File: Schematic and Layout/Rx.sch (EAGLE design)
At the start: 19 parts

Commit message: Add files via upload
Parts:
- U$10: value RES -> 100
- U$11, U$4: value RES -> 10K
- U$13: value LED_1206 -> LED_12V
- U$14: value CAP -> 470uF
- U$15: value RES -> 330
- U$16, U$6: value RES -> 1K
- U$18: value POWER_CONN -> 5V-12V
- U$20: value DIODE_Z_1005 -> 15V_Z
- U$5, U$7: value RES -> 100K
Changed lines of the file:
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@@
 <part name="GND1" library="supply1" deviceset="GND" device=""/>
 <part name="U$3" library="Gas_Sensor_Lib_v1" deviceset="DIODE_1206" device=""/>
-<part name="U$4" library="Gas_Sensor_Lib_v1" deviceset="RES" device=""/>
-<part name="U$5" library="Gas_Sensor_Lib_v1" deviceset="RES" device=""/>
-<part name="U$6" library="Gas_Sensor_Lib_v1" deviceset="RES" device=""/>
-<part name="U$7" library="Gas_Sensor_Lib_v1" deviceset="RES" device=""/>
+<part name="U$4" library="Gas_Sensor_Lib_v1" deviceset="RES" device="" value="10K"/>
+<part name="U$5" library="Gas_Sensor_Lib_v1" deviceset="RES" device="" value="100K"/>
+<part name="U$6" library="Gas_Sensor_Lib_v1" deviceset="RES" device="" value="1K"/>
+<part name="U$7" library="Gas_Sensor_Lib_v1" deviceset="RES" device="" value="100K"/>
 <part name="U$8" library="Gas_Sensor_Lib_v1" deviceset="POWER_CONN" device=""/>
 <part name="GND2" library="supply1" deviceset="GND" device=""/>
 <part name="U$9" library="Gas_Sensor_Lib_v1" deviceset="ESP8266" device=""/>
 <part name="GND3" library="supply1" deviceset="GND" device=""/>
-<part name="U$10" library="Gas_Sensor_Lib_v1" deviceset="RES" device=""/>
-<part name="U$11" library="Gas_Sensor_Lib_v1" deviceset="RES" device=""/>
+<part name="U$10" library="Gas_Sensor_Lib_v1" deviceset="RES" device="" value="100"/>
+<part name="U$11" library="Gas_Sensor_Lib_v1" deviceset="RES" device="" value="10K"/>
 <part name="U$12" library="Gas_Sensor_Lib_v1" deviceset="BUTTON" device=""/>
-<part name="U$13" library="Gas_Sensor_Lib_v1" deviceset="LED_1206" device=""/>
+<part name="U$13" library="Gas_Sensor_Lib_v1" deviceset="LED_1206" device="" value="LED_12V"/>
 <part name="GND4" library="supply1" deviceset="GND" device=""/>
-<part name="U$14" library="Gas_Sensor_Lib_v1" deviceset="CAP" device=""/>
-<part name="U$15" library="Gas_Sensor_Lib_v1" deviceset="RES" device=""/>
-<part name="U$16" library="Gas_Sensor_Lib_v1" deviceset="RES" device=""/>
+<part name="U$14" library="Gas_Sensor_Lib_v1" deviceset="CAP" device="" value="470uF"/>
+<part name="U$15" library="Gas_Sensor_Lib_v1" deviceset="RES" device="" value="330"/>
+<part name="U$16" library="Gas_Sensor_Lib_v1" deviceset="RES" device="" value="1K"/>
 <part name="U$17" library="Gas_Sensor_Lib_v1" deviceset="DIODE_1206" device=""/>
-<part name="U$18" library="Gas_Sensor_Lib_v1" deviceset="POWER_CONN" device=""/>
-<part name="U$20" library="Gas_Sensor_Lib_v1" deviceset="DIODE_Z_1005" device=""/>
+<part name="U$18" library="Gas_Sensor_Lib_v1" deviceset="POWER_CONN" device="" value="5V-12V"/>
+<part name="U$20" library="Gas_Sensor_Lib_v1" deviceset="DIODE_Z_1005" device="" value="15V_Z"/>
 </parts>
 <sheets>

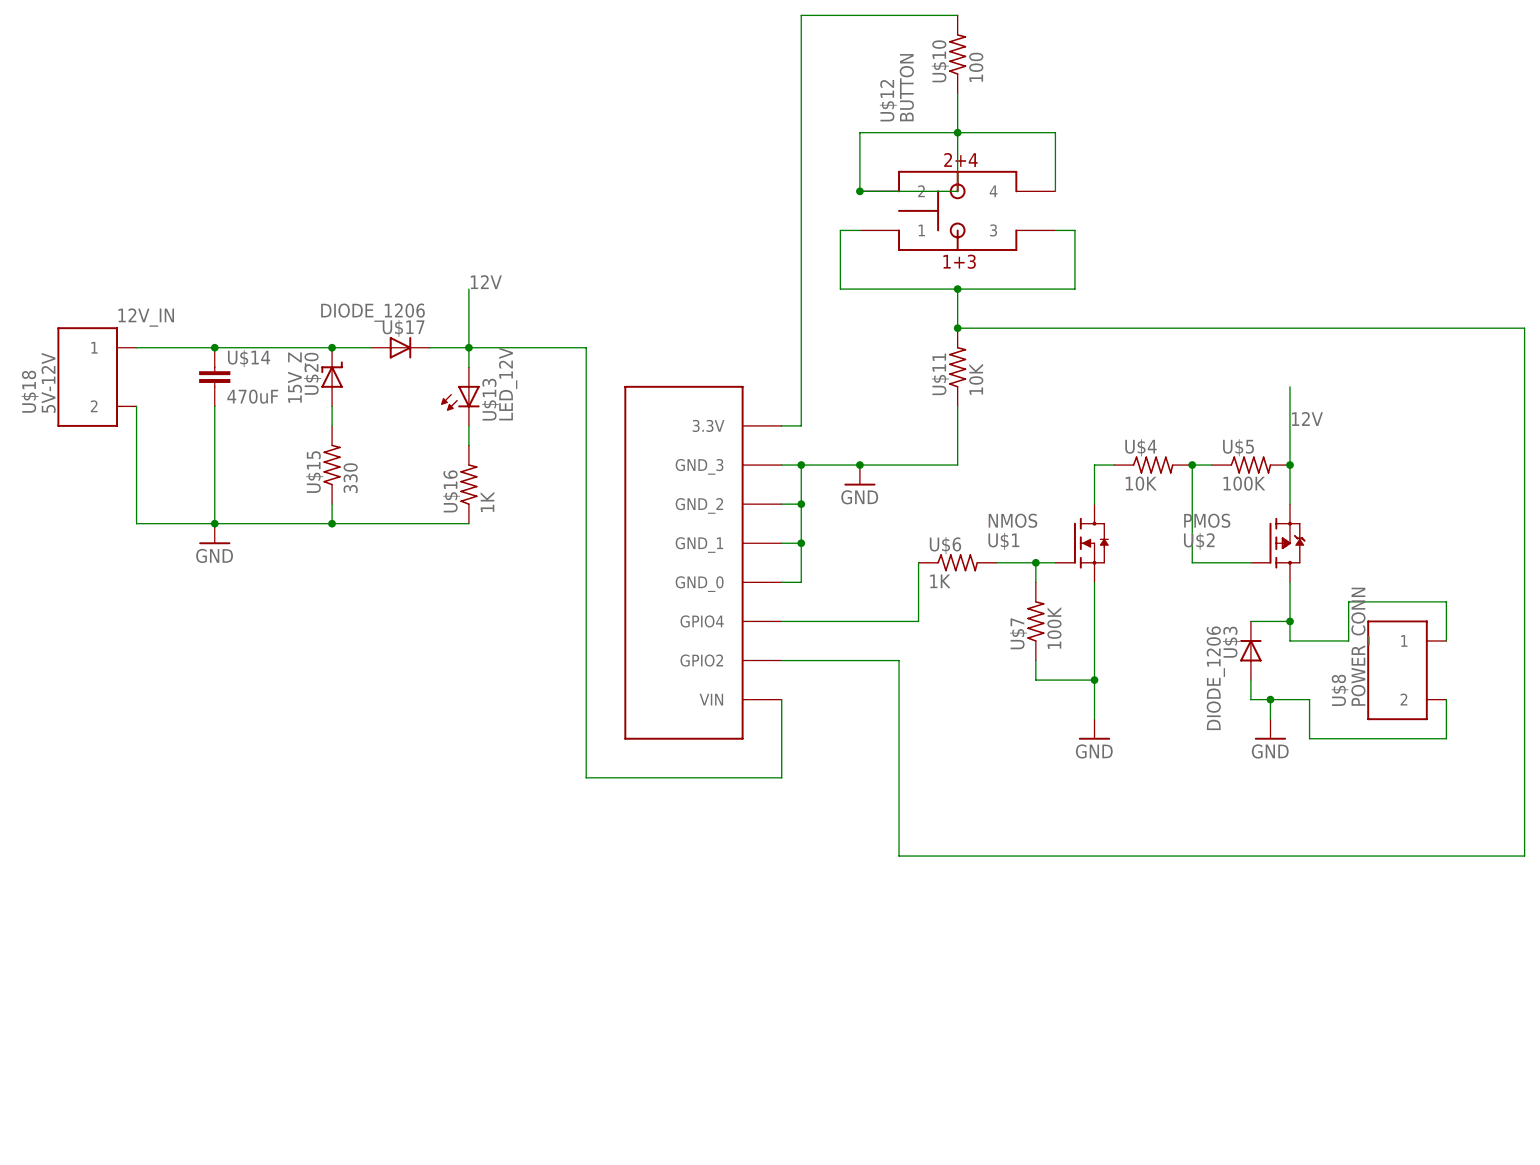
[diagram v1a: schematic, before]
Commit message: Add files via upload
I added an output LED on the receiver side and put some silkscreen on the bottom with our first names. 
I also added "RESET" next to the button on the silkscreen for the rx.
Input capacitance decreased to 10uF. Too expensive to get 470uF.
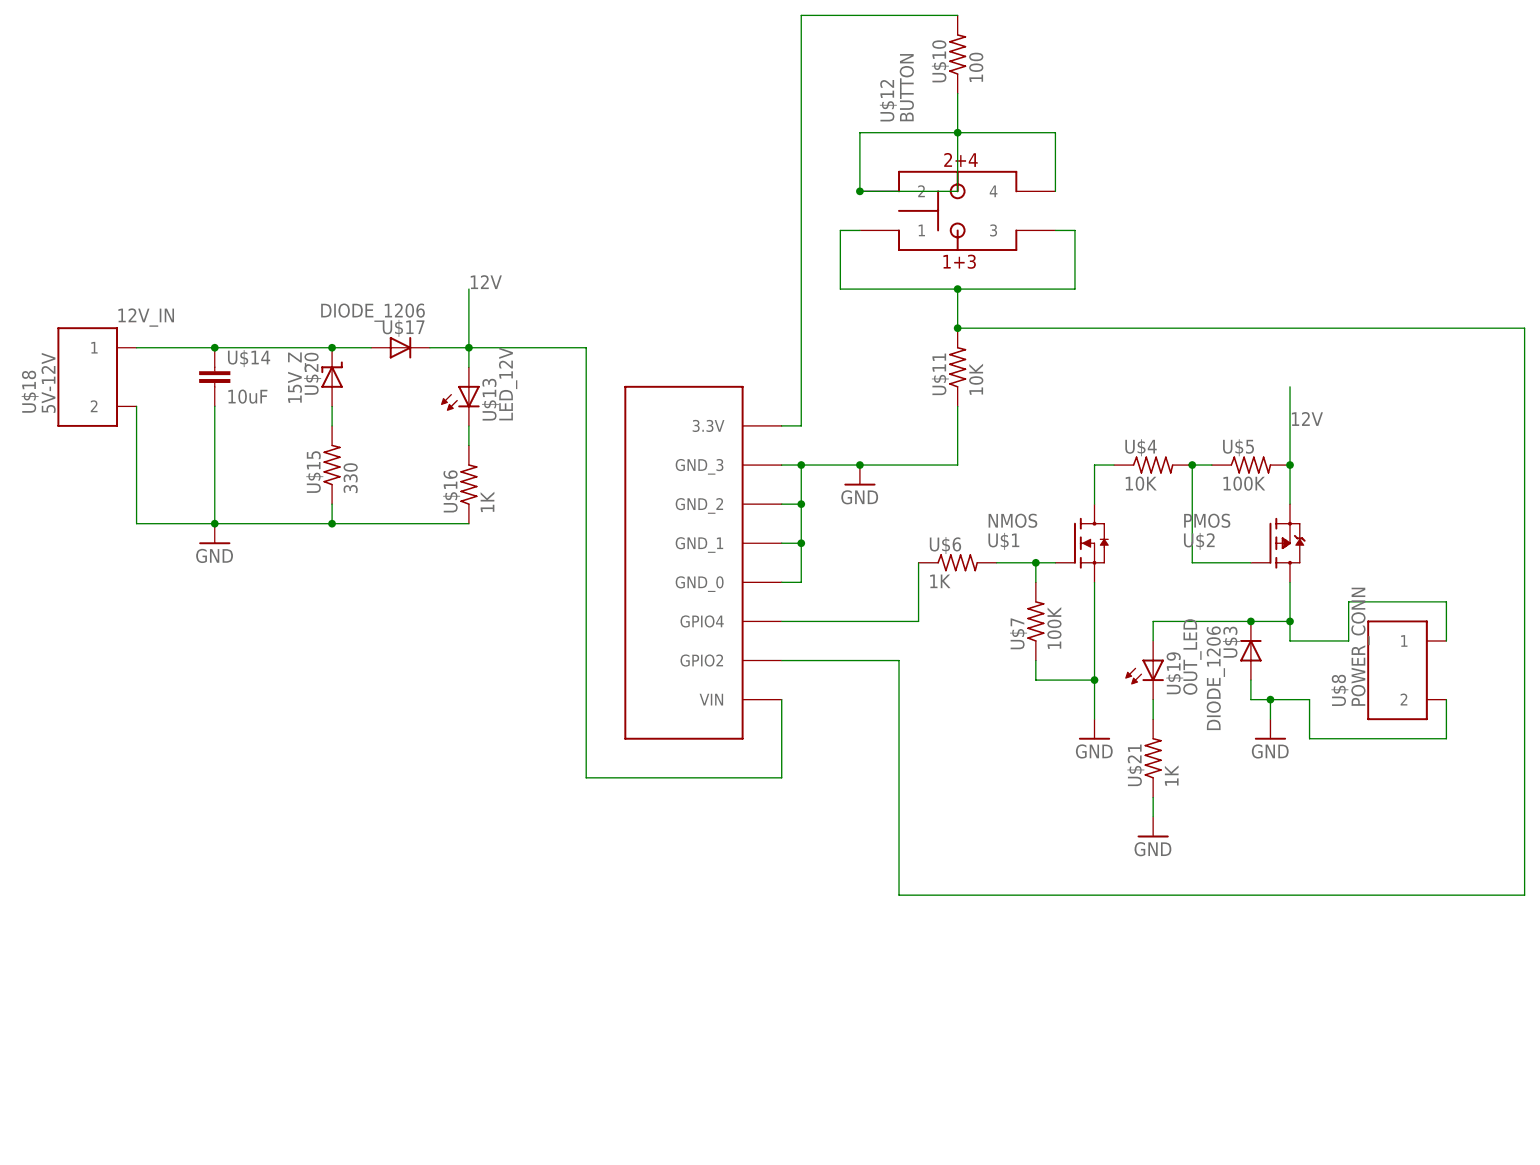
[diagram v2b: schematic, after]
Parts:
- added U$19: OUT_LED, Gas_Sensor_Lib_v1:LED_1206
- added U$21: 1K, Gas_Sensor_Lib_v1:RES
- U$14: value 470uF -> 10uF
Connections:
- new net N$5: U$19.LO, U$21.2
- net GND: now also U$21.1
- net N$6: now also U$19.HI
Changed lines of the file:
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@@
 <part name="U$13" library="Gas_Sensor_Lib_v1" deviceset="LED_1206" device="" value="LED_12V"/>
 <part name="GND4" library="supply1" deviceset="GND" device=""/>
-<part name="U$14" library="Gas_Sensor_Lib_v1" deviceset="CAP" device="" value="470uF"/>
+<part name="U$14" library="Gas_Sensor_Lib_v1" deviceset="CAP" device="" value="10uF"/>
 <part name="U$15" library="Gas_Sensor_Lib_v1" deviceset="RES" device="" value="330"/>
 <part name="U$16" library="Gas_Sensor_Lib_v1" deviceset="RES" device="" value="1K"/>
@@
 <part name="U$18" library="Gas_Sensor_Lib_v1" deviceset="POWER_CONN" device="" value="5V-12V"/>
 <part name="U$20" library="Gas_Sensor_Lib_v1" deviceset="DIODE_Z_1005" device="" value="15V_Z"/>
+<part name="U$19" library="Gas_Sensor_Lib_v1" deviceset="LED_1206" device="" value="OUT_LED"/>
+<part name="U$21" library="Gas_Sensor_Lib_v1" deviceset="RES" device="" value="1K"/>
+<part name="GND5" library="supply1" deviceset="GND" device=""/>
 </parts>
 <sheets>
@@
 <instance part="U$18" gate="G$1" x="-73.66" y="55.88"/>
 <instance part="U$20" gate="G$1" x="-43.18" y="55.88" rot="R180"/>
+<instance part="U$19" gate="G$1" x="63.5" y="20.32"/>
+<instance part="U$21" gate="G$1" x="63.5" y="7.62" rot="R90"/>
+<instance part="GND5" gate="1" x="63.5" y="-2.54"/>
 </instances>
 <busses>
@@
 <wire x1="-68.58" y1="38.1" x2="-58.42" y2="38.1" width="0.1524" layer="91"/>
 </segment>
+<segment>
+<pinref part="U$21" gate="G$1" pin="1"/>
+<pinref part="GND5" gate="1" pin="GND"/>
+<wire x1="63.5" y1="2.54" x2="63.5" y2="0" width="0.1524" layer="91"/>
+</segment>
 </net>
 <net name="N$3" class="0">
@@
 <wire x1="88.9" y1="27.94" x2="101.6" y2="27.94" width="0.1524" layer="91"/>
 <wire x1="101.6" y1="27.94" x2="101.6" y2="22.86" width="0.1524" layer="91"/>
+<pinref part="U$19" gate="G$1" pin="HI"/>
+<wire x1="63.5" y1="22.86" x2="63.5" y2="25.4" width="0.1524" layer="91"/>
+<wire x1="63.5" y1="25.4" x2="76.2" y2="25.4" width="0.1524" layer="91"/>
+<junction x="76.2" y="25.4"/>
 </segment>
 </net>
@@
 <pinref part="U$9" gate="G$1" pin="GPIO2"/>
 <wire x1="15.24" y1="20.32" x2="30.48" y2="20.32" width="0.1524" layer="91"/>
-<wire x1="30.48" y1="20.32" x2="30.48" y2="-5.08" width="0.1524" layer="91"/>
-<wire x1="30.48" y1="-5.08" x2="111.76" y2="-5.08" width="0.1524" layer="91"/>
-<wire x1="111.76" y1="-5.08" x2="111.76" y2="63.5" width="0.1524" layer="91"/>
+<wire x1="30.48" y1="20.32" x2="30.48" y2="-10.16" width="0.1524" layer="91"/>
+<wire x1="30.48" y1="-10.16" x2="111.76" y2="-10.16" width="0.1524" layer="91"/>
+<wire x1="111.76" y1="-10.16" x2="111.76" y2="63.5" width="0.1524" layer="91"/>
 <pinref part="U$11" gate="G$1" pin="2"/>
 <wire x1="38.1" y1="63.5" x2="111.76" y2="63.5" width="0.1524" layer="91"/>
@@
 </segment>
 </net>
+<net name="N$5" class="0">
+<segment>
+<pinref part="U$19" gate="G$1" pin="LO"/>
+<pinref part="U$21" gate="G$1" pin="2"/>
+<wire x1="63.5" y1="15.24" x2="63.5" y2="12.7" width="0.1524" layer="91"/>
+</segment>
+</net>
